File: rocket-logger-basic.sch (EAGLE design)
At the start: 61 parts, among them IC1 CC430F513X, Q2 MOSFET-PCHANNEL, U2 MAX1555, U3 MCP73831, X1 0896BM15A0001, X2 USB-MICROB, X3 SMA-142-0701-801/806

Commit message: basic logger done
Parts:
- removed JP1: (no value), SparkFun:M02-JST-2MM-SMT
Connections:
- net GND: no longer JP1.1
- net N$2: no longer JP1.2
- net N$25: now also R4.2
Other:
- moved on the sheet: U$1, U$2
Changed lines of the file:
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@@
 <parts>
 <part name="U$4" library="Mine" deviceset="MPL5115A2" device=""/>
-<part name="JP1" library="SparkFun" deviceset="M02" device="-JST-2MM-SMT"/>
 <part name="IC1" library="Mine" deviceset="CC430F513X" device=""/>
 <part name="X1" library="Mine" deviceset="0896BM15A0001" device=""/>
@@
 <part name="C11" library="resistor" deviceset="C-EU" device="C0402"/>
 <part name="GND14" library="SparkFun" deviceset="GND" device=""/>
-<part name="GND15" library="SparkFun" deviceset="GND" device=""/>
 <part name="GND16" library="SparkFun" deviceset="GND" device=""/>
 <part name="+3V1" library="supply1" deviceset="+3V3" device=""/>
@@
 <sheet>
 <plain>
-<text x="144.78" y="248.92" size="1.778" layer="91">CHECK!!!</text>
+<text x="152.4" y="255.27" size="1.778" layer="91">CHECK!!!</text>
 <text x="209.55" y="153.67" size="1.778" layer="91">connect -&gt; ?</text>
 <text x="232.664" y="144.018" size="1.778" layer="91">3</text>
@@
 <instances>
 <instance part="U$4" gate="G$1" x="240.03" y="161.29"/>
-<instance part="JP1" gate="G$1" x="147.32" y="243.84" rot="R270"/>
 <instance part="IC1" gate="G$1" x="53.34" y="160.02"/>
 <instance part="X1" gate="G$1" x="-29.21" y="170.18" rot="MR0"/>
@@
 <instance part="C11" gate="G$1" x="105.41" y="233.68" rot="MR0"/>
 <instance part="GND14" gate="1" x="105.41" y="238.76" smashed="yes" rot="R180"/>
-<instance part="GND15" gate="1" x="147.32" y="233.68" smashed="yes"/>
 <instance part="GND16" gate="1" x="177.8" y="218.44" smashed="yes" rot="R90"/>
 <instance part="+3V1" gate="G$1" x="186.69" y="228.6" rot="R270"/>
@@
 <instance part="Q2" gate="G$1" x="137.16" y="294.64" rot="MR90"/>
 <instance part="R12" gate="G$1" x="138.43" y="267.97" rot="R270"/>
-<instance part="U$1" gate="G$1" x="160.02" y="248.92" rot="R270"/>
-<instance part="U$2" gate="G$1" x="170.18" y="248.92" rot="R270"/>
-<instance part="GND31" gate="1" x="172.72" y="238.76" smashed="yes"/>
-<instance part="GND33" gate="1" x="162.56" y="238.76" smashed="yes"/>
+<instance part="U$1" gate="G$1" x="149.86" y="248.92" rot="R270"/>
+<instance part="U$2" gate="G$1" x="162.56" y="248.92" rot="R270"/>
+<instance part="GND31" gate="1" x="165.1" y="238.76" smashed="yes"/>
+<instance part="GND33" gate="1" x="152.4" y="238.76" smashed="yes"/>
 <instance part="U3" gate="G$1" x="119.38" y="226.06"/>
 <instance part="R13" gate="G$1" x="132.08" y="214.63" rot="R270"/>
@@
 </segment>
 <segment>
-<pinref part="JP1" gate="G$1" pin="1"/>
-<pinref part="GND15" gate="1" pin="GND"/>
-</segment>
-<segment>
 <pinref part="IC2" gate="G$1" pin="GND"/>
 <pinref part="GND16" gate="1" pin="GND"/>
@@
 <net name="N$2" class="0">
 <segment>
-<pinref part="JP1" gate="G$1" pin="2"/>
 <wire x1="139.7" y1="228.6" x2="149.86" y2="228.6" width="0.1524" layer="91"/>
 <wire x1="149.86" y1="236.22" x2="149.86" y2="228.6" width="0.1524" layer="91"/>
@@
 <pinref part="U$2" gate="G$1" pin="1"/>
 <wire x1="139.7" y1="214.63" x2="139.7" y2="228.6" width="0.1524" layer="91"/>
-<wire x1="170.18" y1="241.3" x2="170.18" y2="236.22" width="0.1524" layer="91"/>
-<wire x1="170.18" y1="236.22" x2="160.02" y2="236.22" width="0.1524" layer="91"/>
+<wire x1="162.56" y1="241.3" x2="162.56" y2="236.22" width="0.1524" layer="91"/>
+<wire x1="162.56" y1="236.22" x2="149.86" y2="236.22" width="0.1524" layer="91"/>
 <pinref part="U$1" gate="G$1" pin="1"/>
-<wire x1="160.02" y1="236.22" x2="149.86" y2="236.22" width="0.1524" layer="91"/>
-<wire x1="160.02" y1="241.3" x2="160.02" y2="236.22" width="0.1524" layer="91"/>
+<wire x1="149.86" y1="241.3" x2="149.86" y2="236.22" width="0.1524" layer="91"/>
 <junction x="149.86" y="236.22"/>
-<junction x="160.02" y="236.22"/>
 <pinref part="U3" gate="G$1" pin="VBAT"/>
 <wire x1="129.54" y1="228.6" x2="139.7" y2="228.6" width="0.1524" layer="91"/>
@@
 <net name="N$16" class="0">
 <segment>
-<wire x1="80.01" y1="149.86" x2="77.47" y2="147.32" width="0.1524" layer="91"/>
 <pinref part="IC1" gate="G$1" pin="P2.3"/>
-<wire x1="66.04" y1="144.78" x2="77.47" y2="144.78" width="0.1524" layer="91"/>
-<wire x1="77.47" y1="144.78" x2="77.47" y2="147.32" width="0.1524" layer="91"/>
+<wire x1="66.04" y1="144.78" x2="74.93" y2="144.78" width="0.1524" layer="91"/>
+<wire x1="74.93" y1="144.78" x2="80.01" y2="149.86" width="0.1524" layer="91"/>
 <pinref part="LED1" gate="G$1" pin="A"/>
 <wire x1="97.79" y1="149.86" x2="80.01" y2="149.86" width="0.1524" layer="91"/>
@@
 <wire x1="154.94" y1="214.63" x2="154.94" y2="223.52" width="0.1524" layer="91"/>
 <junction x="157.48" y="209.55"/>
-</segment>
-</net>
+<pinref part="R4" gate="G$1" pin="2"/>
+<wire x1="157.48" y1="207.01" x2="157.48" y2="209.55" width="0.1524" layer="91"/>
+</segment>
+</net>

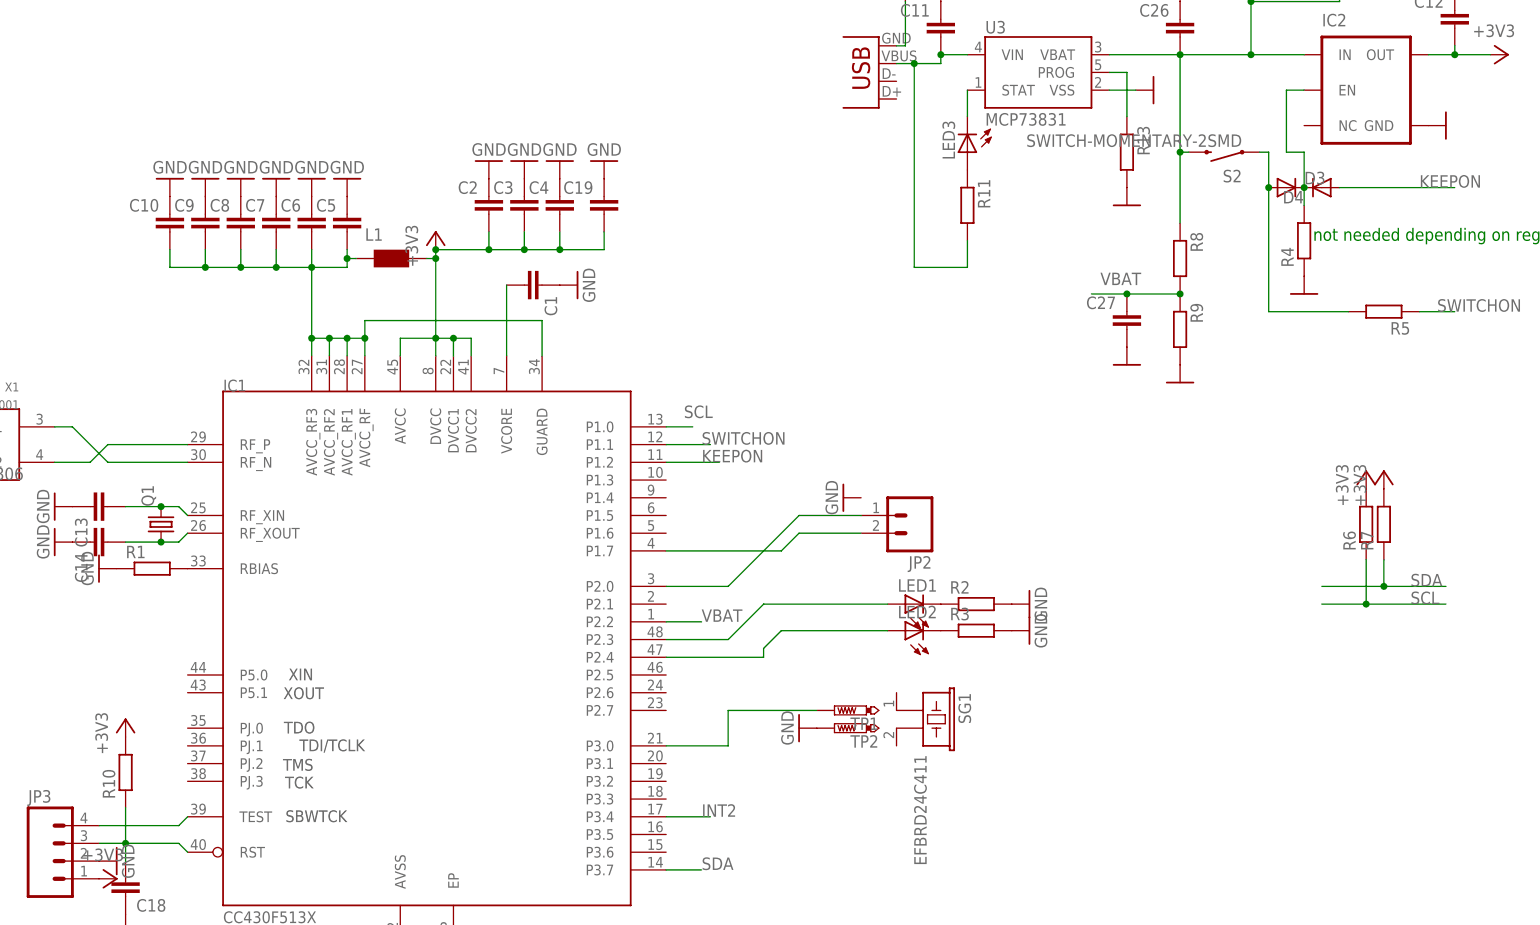
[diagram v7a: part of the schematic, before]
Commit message: added part values
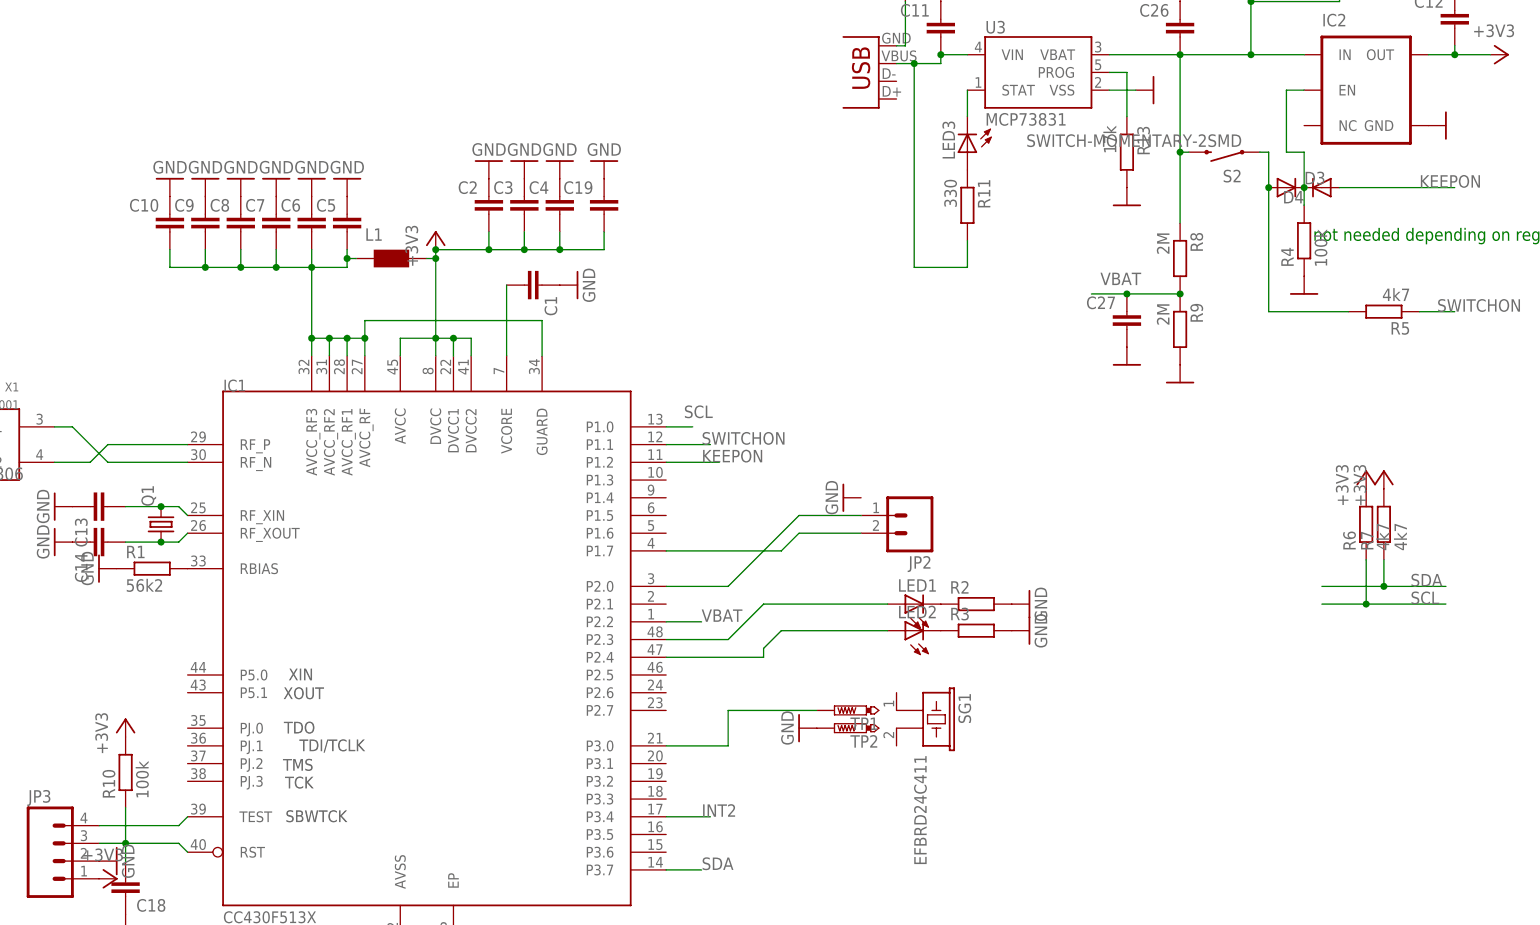
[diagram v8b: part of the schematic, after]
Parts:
- R1: value (none) -> 56k2
- R10, R4: value (none) -> 100k
- R11: value (none) -> 330
- R13: value (none) -> 17k
- R5, R6, R7: value (none) -> 4k7
- R8, R9: value (none) -> 2M
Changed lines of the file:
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@@
 <?xml version="1.0" encoding="utf-8"?>
 <!DOCTYPE eagle SYSTEM "eagle.dtd">
-<eagle version="6.2">
+<eagle version="6.5.0">
 <drawing>
 <settings>
@@
 <setting verticaltext="up"/>
 </settings>
-<grid distance="0.05" unitdist="inch" unit="inch" style="lines" multiple="1" display="no" altdistance="0.01" altunitdist="inch" altunit="inch"/>
+<grid distance="0.1" unitdist="inch" unit="inch" style="lines" multiple="1" display="no" altdistance="0.01" altunitdist="inch" altunit="inch"/>
 <layers>
 <layer number="1" name="Top" color="4" fill="1" visible="no" active="no"/>
@@
 <part name="GND19" library="supply1" deviceset="GND" device=""/>
 <part name="GND20" library="supply1" deviceset="GND" device=""/>
-<part name="R1" library="rcl" deviceset="R-EU_" device="R0402"/>
+<part name="R1" library="rcl" deviceset="R-EU_" device="R0402" value="56k2"/>
 <part name="GND21" library="supply1" deviceset="GND" device=""/>
 <part name="X3" library="con-coax" deviceset="SMA-" device="142-0701-801/806"/>
@@
 <part name="C17" library="resistor" deviceset="C-EU" device="C0402"/>
 <part name="GND28" library="SparkFun" deviceset="GND" device=""/>
-<part name="R4" library="rcl" deviceset="R-EU_" device="R0402"/>
+<part name="R4" library="rcl" deviceset="R-EU_" device="R0402" value="100k"/>
 <part name="GND43" library="SparkFun" deviceset="GND" device=""/>
 <part name="+3V4" library="supply1" deviceset="+3V3" device=""/>
@@
 <part name="JP2" library="SparkFun" deviceset="M02" device="PTH"/>
 <part name="+3V9" library="supply1" deviceset="+3V3" device=""/>
-<part name="R6" library="rcl" deviceset="R-EU_" device="R0402"/>
-<part name="R7" library="rcl" deviceset="R-EU_" device="R0402"/>
+<part name="R6" library="rcl" deviceset="R-EU_" device="R0402" value="4k7"/>
+<part name="R7" library="rcl" deviceset="R-EU_" device="R0402" value="4k7"/>
 <part name="+3V10" library="supply1" deviceset="+3V3" device=""/>
 <part name="+3V11" library="supply1" deviceset="+3V3" device=""/>
 <part name="D3" library="diode" deviceset="DIODE-" device="SOD523"/>
 <part name="D4" library="diode" deviceset="DIODE-" device="SOD523"/>
-<part name="R5" library="rcl" deviceset="R-EU_" device="R0402"/>
+<part name="R5" library="rcl" deviceset="R-EU_" device="R0402" value="4k7"/>
 <part name="SG1" library="buzzer" deviceset="EFB?" device="RD24C411"/>
 <part name="C26" library="resistor" deviceset="C-EU" device="C0402"/>
@@
 <part name="TP2" library="testpad" deviceset="PTR1" device="B1,27"/>
 <part name="GND47" library="supply1" deviceset="GND" device=""/>
-<part name="R8" library="rcl" deviceset="R-EU_" device="R0402"/>
-<part name="R9" library="rcl" deviceset="R-EU_" device="R0402"/>
+<part name="R8" library="rcl" deviceset="R-EU_" device="R0402" value="2M"/>
+<part name="R9" library="rcl" deviceset="R-EU_" device="R0402" value="2M"/>
 <part name="GND48" library="SparkFun" deviceset="GND" device=""/>
 <part name="C27" library="resistor" deviceset="C-EU" device="C0402"/>
 <part name="GND49" library="SparkFun" deviceset="GND" device=""/>
-<part name="R10" library="rcl" deviceset="R-EU_" device="R0402"/>
+<part name="R10" library="rcl" deviceset="R-EU_" device="R0402" value="100k"/>
 <part name="C18" library="resistor" deviceset="C-EU" device="C0402"/>
 <part name="GND29" library="supply1" deviceset="GND" device=""/>
@@
 <part name="+3V3" library="supply1" deviceset="+3V3" device=""/>
 <part name="JP3" library="SparkFun" deviceset="M04" device="PTH"/>
-<part name="R11" library="rcl" deviceset="R-EU_" device="R0402"/>
+<part name="R11" library="rcl" deviceset="R-EU_" device="R0402" value="330"/>
 <part name="LED3" library="SparkFun" deviceset="LED" device="0603"/>
 <part name="U2" library="SparkFun" deviceset="MAX1555" device=""/>
@@
 <part name="GND33" library="SparkFun" deviceset="GND" device=""/>
 <part name="U3" library="SparkFun-PowerIC" deviceset="MCP73831" device=""/>
-<part name="R13" library="rcl" deviceset="R-EU_" device="R0402"/>
+<part name="R13" library="rcl" deviceset="R-EU_" device="R0402" value="17k"/>
 <part name="GND34" library="SparkFun" deviceset="GND" device=""/>
 <part name="GND35" library="SparkFun" deviceset="GND" device=""/>
